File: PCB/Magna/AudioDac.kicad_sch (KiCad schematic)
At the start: 20 parts, among them U501 CS4344, U602 NE5532

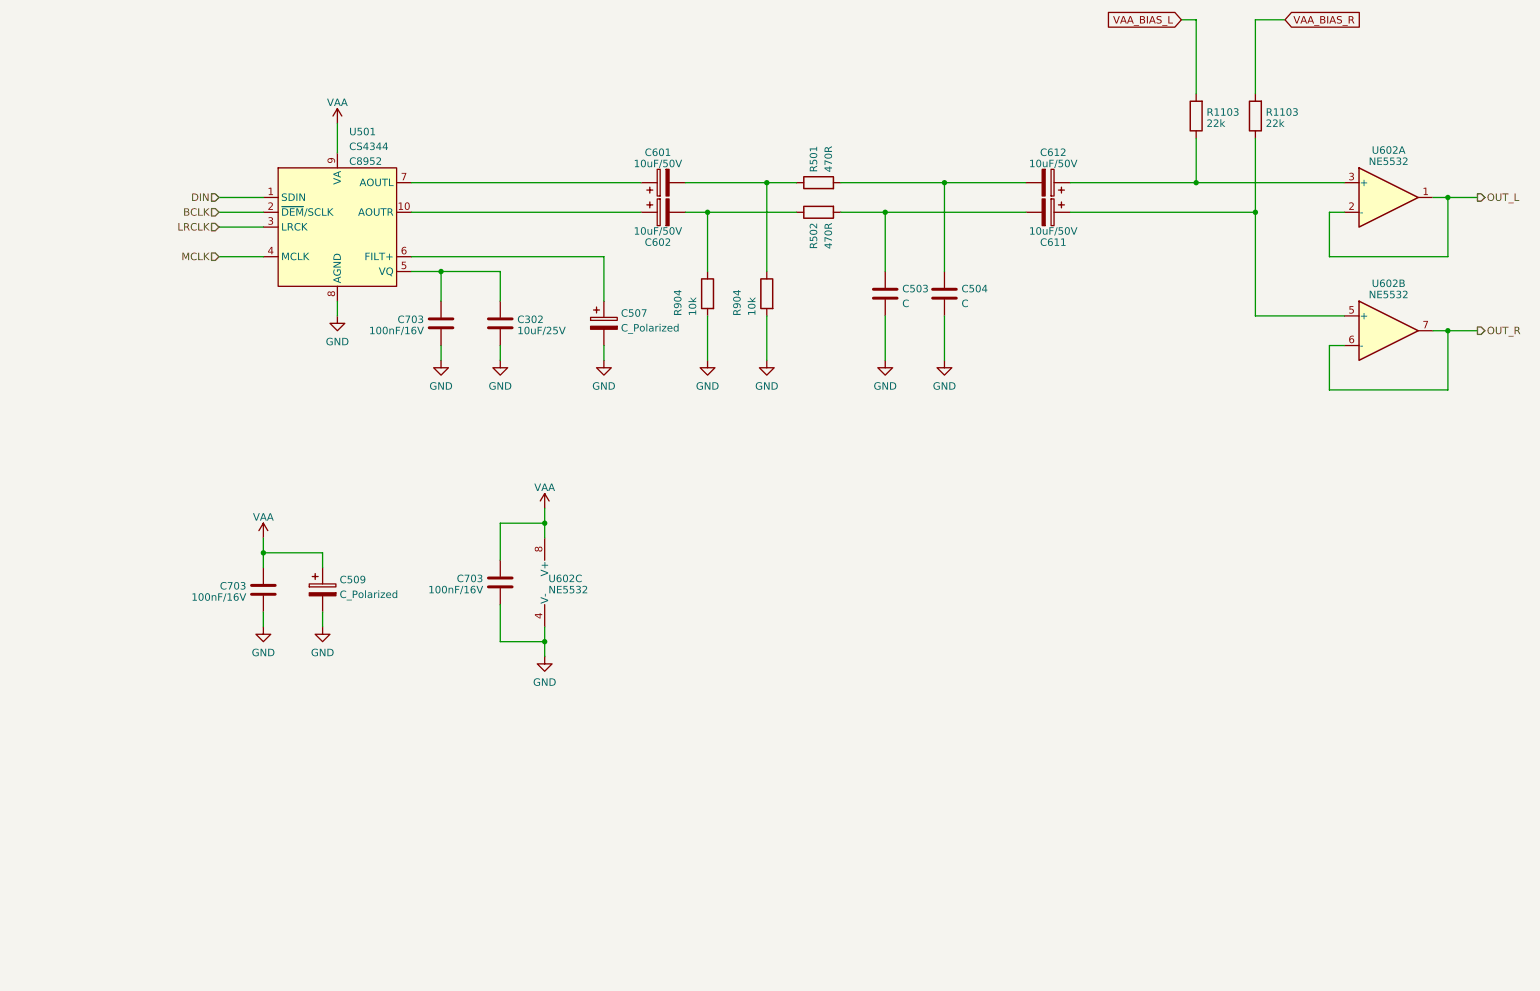
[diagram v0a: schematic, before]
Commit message: Update analogue frontend and add potentiometer interface
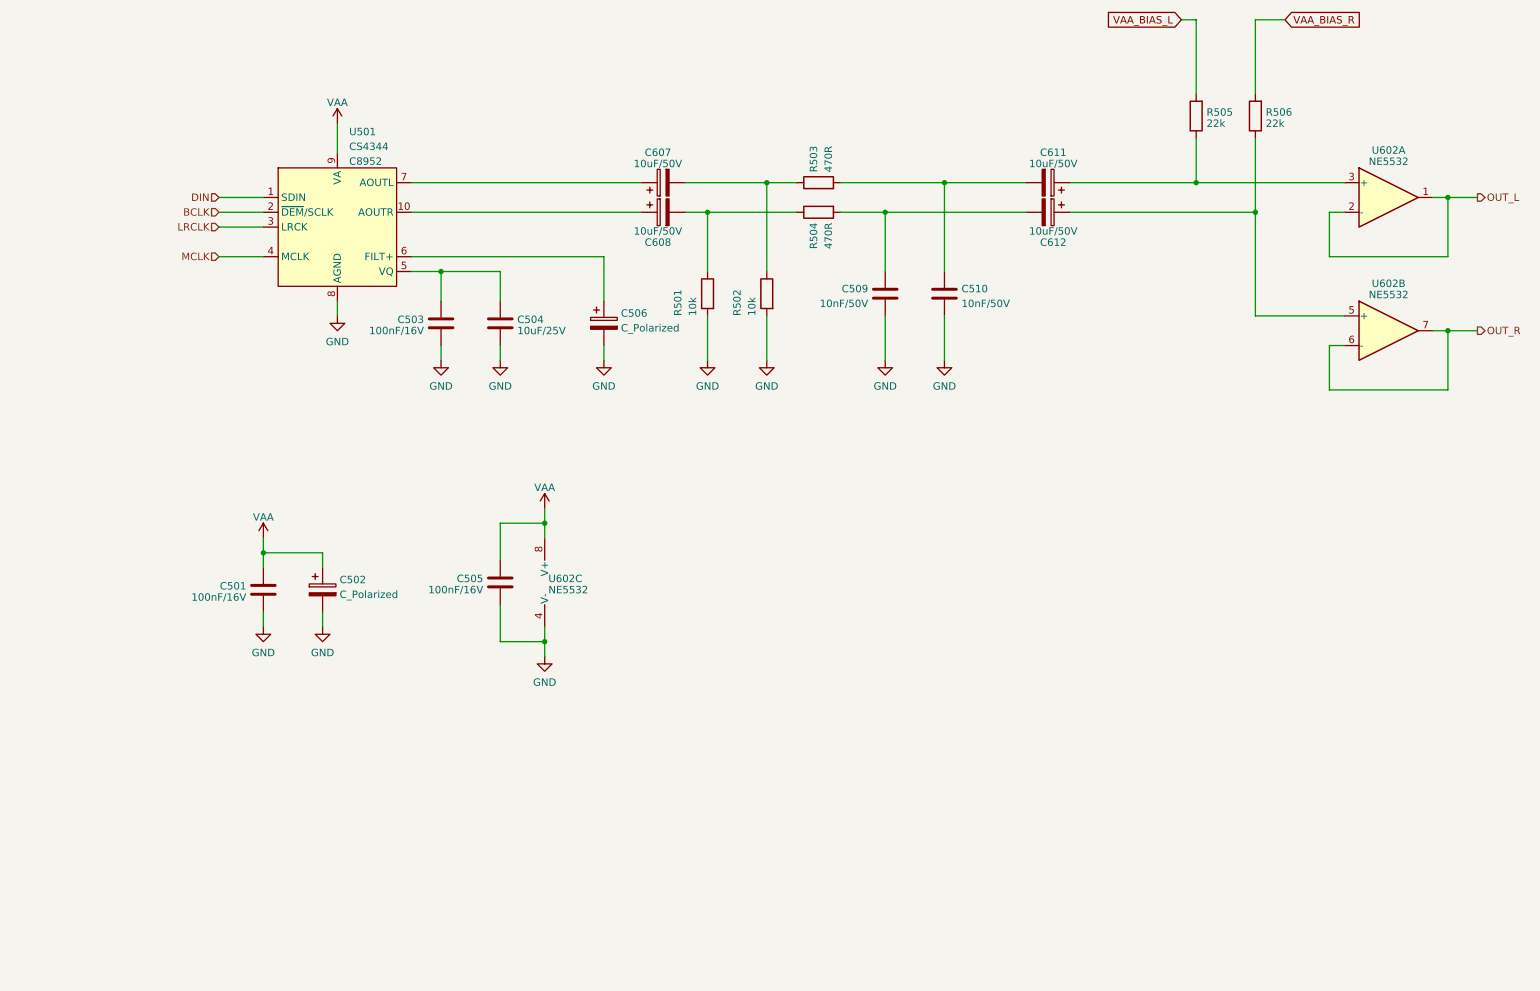
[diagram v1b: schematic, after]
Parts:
- C509: renamed from C503; value C -> 10nF/50V; footprint (none) -> Capacitor_SMD:C_0805_2012Metric_Pad1.18x1.45mm_HandSolder
- C510: renamed from C504; value C -> 10nF/50V; footprint (none) -> Capacitor_SMD:C_0805_2012Metric_Pad1.18x1.45mm_HandSolder; LCSC (none) -> C97905
- renumbered C703 to C501, C509 to C502, C703 to C503, C302 to C504, C703 to C505, C507 to C506, C601 to C607, C602 to C608, C612 to C611, C611 to C612, R904 to R501, R904 to R502, R501 to R503, R502 to R504, R1103 to R505, R1103 to R506

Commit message: Add final touched to all schematics
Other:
- note added: "Decoupling capacitors"
- moved on the sheet: C501, C502, C503, C504, C505, C506, C509, C510, C607, C608, C611, C612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

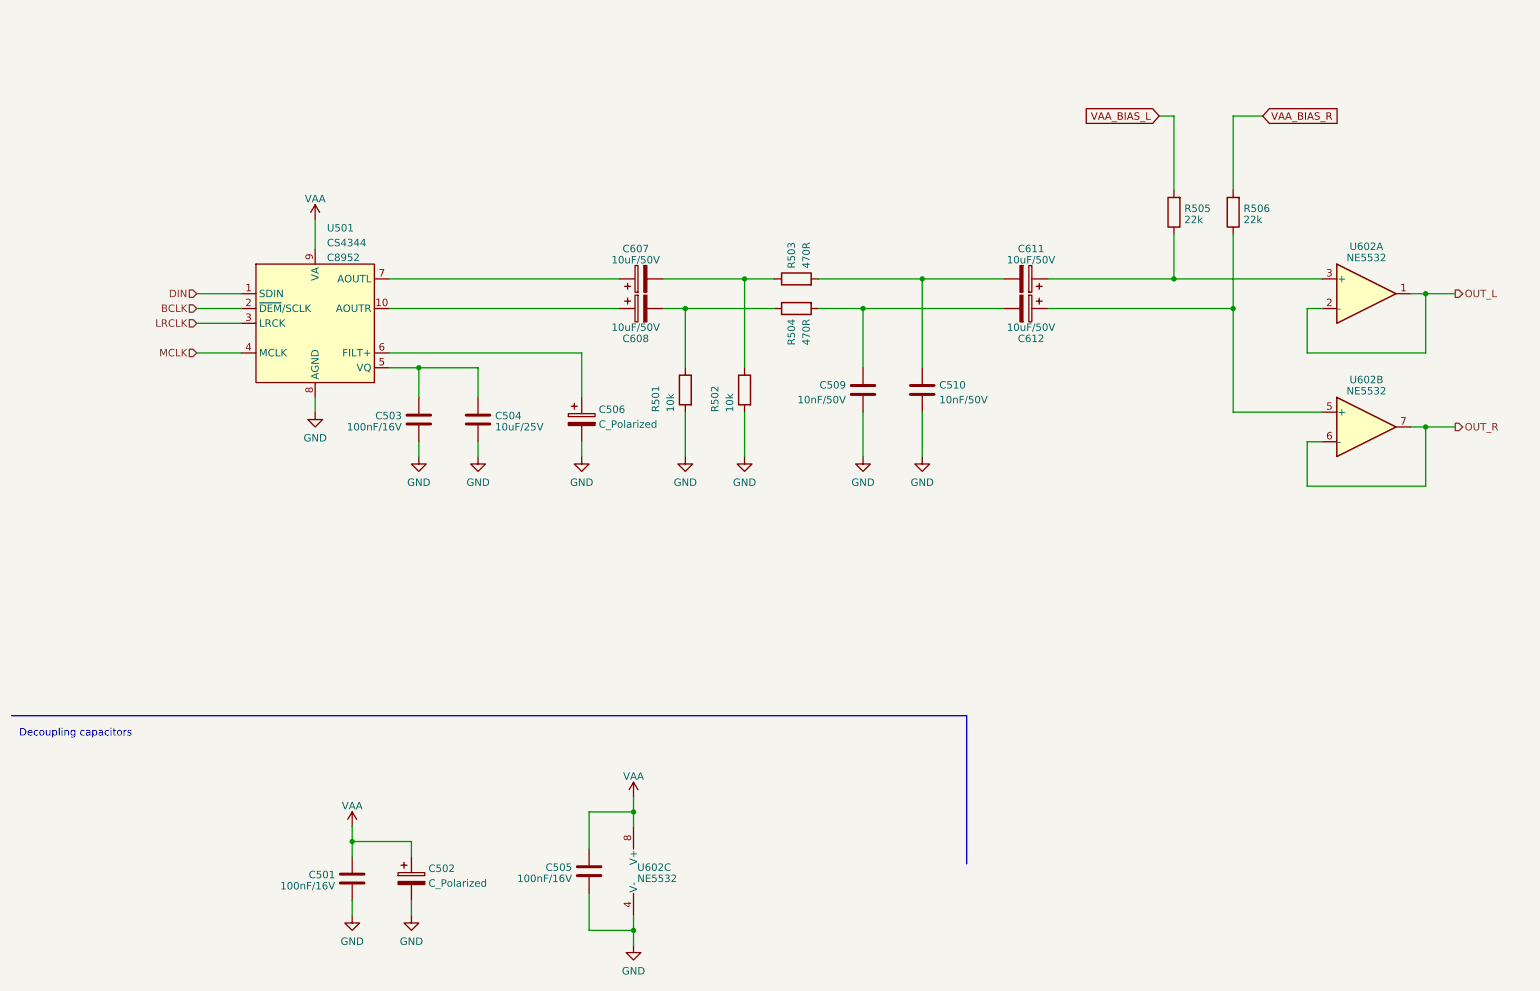
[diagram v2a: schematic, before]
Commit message: Update capacitors to parts in JLC library
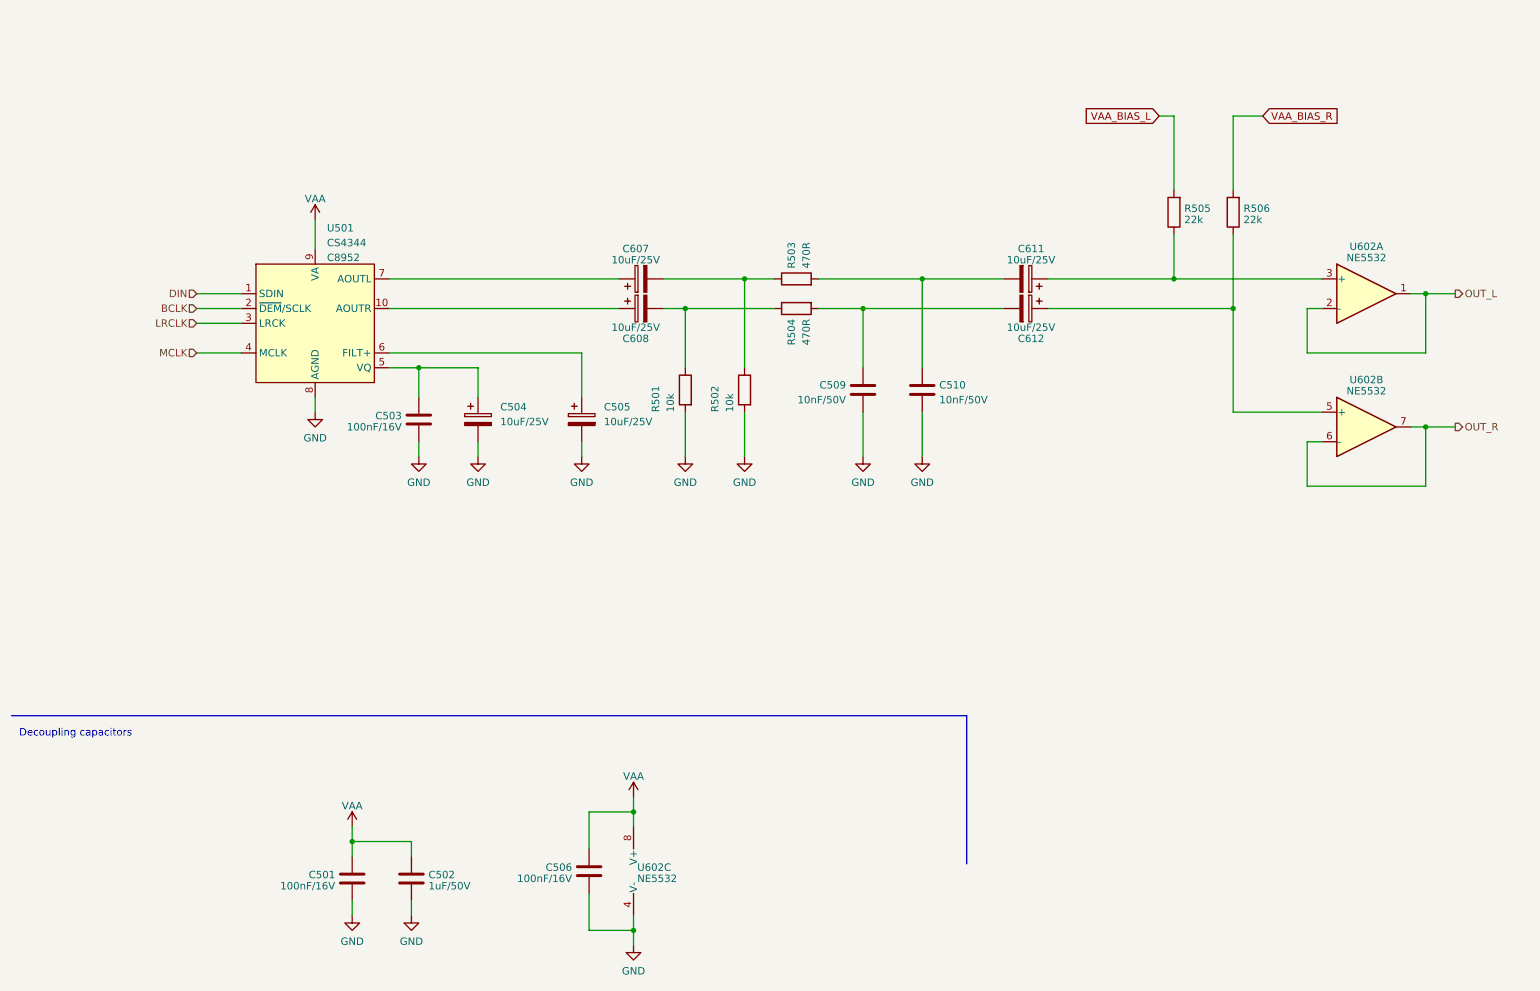
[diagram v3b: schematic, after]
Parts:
- removed C502, C506: C_Polarized, symbol Device:C_Polarized
- removed C504: 10uF/25V, Capacitor_SMD:C_0603_1608Metric, symbol Device:C
- added C502: 1uF/50V, Capacitor_SMD:C_0805_2012Metric, symbol Device:C
- added C504, C505: 10uF/25V, Capacitor_SMD:CP_Elec_4x5.8, symbol Device:C_Polarized
- C501, C503: footprint Capacitor_SMD:C_0402_1005Metric -> Capacitor_SMD:C_0805_2012Metric; LCSC C1525 -> C218638
- C506: renamed from C505; footprint Capacitor_SMD:C_0402_1005Metric -> Capacitor_SMD:C_0805_2012Metric; LCSC C1525 -> C218638
- C509: footprint Capacitor_SMD:C_0805_2012Metric_Pad1.18x1.45mm_HandSolder -> Capacitor_SMD:C_0805_2012Metric; LCSC (none) -> C3908881
- C510: footprint Capacitor_SMD:C_0805_2012Metric_Pad1.18x1.45mm_HandSolder -> Capacitor_SMD:C_0805_2012Metric; LCSC C97905 -> C3908881
- C607, C608, C611, C612: value 10uF/50V -> 10uF/25V; footprint Capacitor_SMD:CP_Elec_6.3x5.8 -> Capacitor_SMD:CP_Elec_4x5.8; Field4 C2164757 -> (none); LCSC (none) -> C2163094
- R501, R502: LCSC C217687 -> (none)
- R503, R504: LCSC C705779 -> (none)
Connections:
- net GND: now also C502.2, C504.2, C505.2
- net VAA: now also C502.1
- net at C503.1, U501.5 (VQ): now also C504.1
- net at U501.6 (FILT+): now also C505.1

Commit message: Select parts for all components
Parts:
- R501, R502: footprint Resistor_SMD:R_0603_1608Metric -> Resistor_SMD:R_0805_2012Metric; LCSC (none) -> C17414
- R503, R504: footprint Resistor_SMD:R_0603_1608Metric -> Resistor_SMD:R_0805_2012Metric_Pad1.20x1.40mm_HandSolder; LCSC (none) -> C706320
- R505, R506: footprint (none) -> Resistor_SMD:R_0805_2012Metric; LCSC (none) -> C479095
- U602: LCSC (none) -> C7426
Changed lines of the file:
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@@
       (effects (font (size 1.27 1.27)) (justify right))
     )
-    (property "Footprint" "" (at 224.028 53.34 90)
+    (property "Footprint" "Resistor_SMD:R_0805_2012Metric" (at 224.028 53.34 90)
       (effects (font (size 1.27 1.27)) hide)
     )
@@
       (effects (font (size 1.27 1.27)) hide)
     )
+    (property "LCSC" "C479095" (at 222.25 53.34 0)
+      (effects (font (size 1.27 1.27)) hide)
+    )
     (pin "1")
     (pin "2")
@@
       (effects (font (size 1.27 1.27)) (justify left))
     )
-    (property "Footprint" "Resistor_SMD:R_0603_1608Metric" (at 147.32 66.548 90)
+    (property "Footprint" "Resistor_SMD:R_0805_2012Metric_Pad1.20x1.40mm_HandSolder" (at 147.32 66.548 90)
       (effects (font (size 1.27 1.27)) hide)
     )
@@
       (effects (font (size 1.27 1.27)) hide)
     )
-    (property "LCSC" "" (at 147.32 64.77 0)
+    (property "LCSC" "C706320" (at 147.32 64.77 0)
       (effects (font (size 1.27 1.27)) hide)
     )
@@
       (effects (font (size 1.27 1.27)) (justify left))
     )
-    (property "Footprint" "Resistor_SMD:R_0603_1608Metric" (at 130.048 83.82 90)
+    (property "Footprint" "Resistor_SMD:R_0805_2012Metric" (at 130.048 83.82 90)
       (effects (font (size 1.27 1.27)) hide)
     )
@@
       (effects (font (size 1.27 1.27)) hide)
     )
-    (property "LCSC" "" (at 128.27 83.82 0)
+    (property "LCSC" "C17414" (at 128.27 83.82 0)
       (effects (font (size 1.27 1.27)) hide)
     )
@@
       (effects (font (size 1.27 1.27)) (justify right))
     )
-    (property "Footprint" "" (at 213.868 53.34 90)
+    (property "Footprint" "Resistor_SMD:R_0805_2012Metric" (at 213.868 53.34 90)
       (effects (font (size 1.27 1.27)) hide)
     )
     (property "Datasheet" "~" (at 212.09 53.34 0)
+      (effects (font (size 1.27 1.27)) hide)
+    )
+    (property "LCSC" "C479095" (at 212.09 53.34 0)
       (effects (font (size 1.27 1.27)) hide)
     )
@@
     )
     (property "Datasheet" "http://www.ti.com/lit/ds/symlink/ne5532.pdf" (at 245.11 90.17 0)
+      (effects (font (size 1.27 1.27)) hide)
+    )
+    (property "LCSC" "C7426" (at 245.11 90.17 0)
       (effects (font (size 1.27 1.27)) hide)
     )
@@
       (effects (font (size 1.27 1.27)) (justify left))
     )
-    (property "Footprint" "Resistor_SMD:R_0603_1608Metric" (at 140.208 83.82 90)
+    (property "Footprint" "Resistor_SMD:R_0805_2012Metric" (at 140.208 83.82 90)
       (effects (font (size 1.27 1.27)) hide)
     )
@@
       (effects (font (size 1.27 1.27)) hide)
     )
-    (property "LCSC" "" (at 138.43 83.82 0)
+    (property "LCSC" "C17414" (at 138.43 83.82 0)
       (effects (font (size 1.27 1.27)) hide)
     )
@@
     )
     (property "Datasheet" "http://www.ti.com/lit/ds/symlink/ne5532.pdf" (at 245.11 67.31 0)
+      (effects (font (size 1.27 1.27)) hide)
+    )
+    (property "LCSC" "C7426" (at 245.11 67.31 0)
       (effects (font (size 1.27 1.27)) hide)
     )
@@
       (effects (font (size 1.27 1.27)) (justify left))
     )
-    (property "Footprint" "Resistor_SMD:R_0603_1608Metric" (at 147.32 68.072 90)
+    (property "Footprint" "Resistor_SMD:R_0805_2012Metric_Pad1.20x1.40mm_HandSolder" (at 147.32 68.072 90)
       (effects (font (size 1.27 1.27)) hide)
     )
@@
       (effects (font (size 1.27 1.27)) hide)
     )
-    (property "LCSC" "" (at 147.32 69.85 0)
+    (property "LCSC" "C706320" (at 147.32 69.85 0)
       (effects (font (size 1.27 1.27)) hide)
     )
@@
       (effects (font (size 1.27 1.27)) hide)
     )
+    (property "LCSC" "C7426" (at 121.92 166.37 0)
+      (effects (font (size 1.27 1.27)) hide)
+    )
